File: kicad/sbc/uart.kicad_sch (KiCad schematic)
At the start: 11 parts, among them J2 DB9, U5 74LS06, U6 16550, U8 MAX232, X2 OSC

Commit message: complete schematics
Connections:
- net ~{JOYPORT_ENABLE}: now reaches U6.38 (~{OUT1})
- no-connect marks 11 -> 10
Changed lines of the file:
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@@
   )
   (no_connect (at 157.48 63.5))
-  (no_connect (at 157.48 60.96))
   (no_connect (at 52.07 92.71))
   (no_connect (at 240.03 137.16))
@@
     (stroke (width 0) (type default))
   )
+  (wire (pts (xy 157.48 60.96) (xy 160.02 60.96))
+    (stroke (width 0) (type default))
+  )
   (wire (pts (xy 245.11 54.61) (xy 250.19 54.61))
     (stroke (width 0) (type default))
@@
     (effects (font (size 1.27 1.27)) (justify left))
   )
+  (hierarchical_label "~{JOYPORT_ENABLE}" (shape output) (at 160.02 60.96 0) (fields_autoplaced)
+    (effects (font (size 1.27 1.27)) (justify left))
+  )

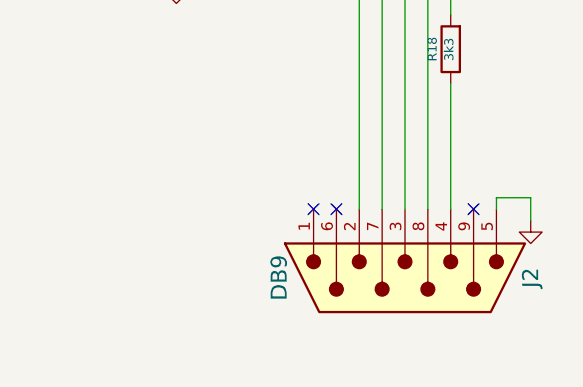
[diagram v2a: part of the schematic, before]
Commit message: fix ERC messages
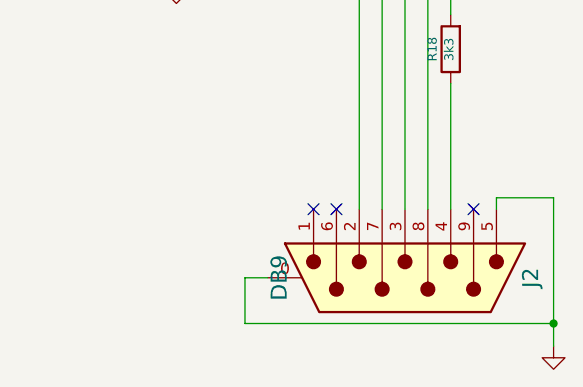
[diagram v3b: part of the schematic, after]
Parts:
- J2: symbol Connector:DB9_Male -> Connector:DE9_Plug_MountingHoles
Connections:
- net GND: now also J2.0 (PAD)
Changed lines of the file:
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@@
   (junction (at 224.79 46.99) (diameter 0) (color 0 0 0 0)
+  )
+  (junction (at 266.7 149.86) (diameter 0) (color 0 0 0 0)
   )
   (junction (at 255.27 67.31) (diameter 0) (color 0 0 0 0)
@@
     (stroke (width 0) (type default))
   )
+  (wire (pts (xy 232.41 149.86) (xy 266.7 149.86))
+    (stroke (width 0) (type default))
+  )
   (wire (pts (xy 224.79 44.45) (xy 224.79 46.99))
     (stroke (width 0) (type default))
@@
     (stroke (width 0) (type default))
   )
+  (wire (pts (xy 266.7 149.86) (xy 266.7 152.4))
+    (stroke (width 0) (type default))
+  )
   (wire (pts (xy 245.11 54.61) (xy 250.19 54.61))
     (stroke (width 0) (type default))
@@
     (stroke (width 0) (type default))
   )
-  (wire (pts (xy 260.35 135.89) (xy 264.16 135.89))
+  (wire (pts (xy 260.35 135.89) (xy 266.7 135.89))
     (stroke (width 0) (type default))
   )
@@
     (stroke (width 0) (type default))
   )
+  (wire (pts (xy 234.95 144.78) (xy 232.41 144.78))
+    (stroke (width 0) (type default))
+  )
   (wire (pts (xy 63.5 130.81) (xy 73.66 130.81))
     (stroke (width 0) (type default))
@@
     (stroke (width 0) (type default))
   )
+  (wire (pts (xy 232.41 144.78) (xy 232.41 149.86))
+    (stroke (width 0) (type default))
+  )
   (wire (pts (xy 106.68 76.2) (xy 95.25 76.2))
     (stroke (width 0) (type default))
@@
     (stroke (width 0) (type default))
   )
-  (wire (pts (xy 264.16 135.89) (xy 264.16 138.43))
+  (wire (pts (xy 266.7 135.89) (xy 266.7 149.86))
     (stroke (width 0) (type default))
   )
@@
     (effects (font (size 1.27 1.27)) (justify left))
   )
-  (symbol (lib_name "VCC_4") (lib_id "power:VCC") (at 73.66 115.57 0) (unit 1)
+  (symbol (lib_id "power:VCC") (at 73.66 115.57 0) (unit 1)
     (in_bom yes) (on_board yes) (dnp no)
     (property "Reference" "#PWR0144" (at 73.66 113.03 0)
@@
     )
   )
-  (symbol (lib_name "GND_2") (lib_id "power:GND") (at 259.08 76.2 0) (unit 1)
+  (symbol (lib_id "power:GND") (at 259.08 76.2 0) (unit 1)
     (in_bom yes) (on_board yes) (dnp no)
     (property "Reference" "#PWR0148" (at 259.08 76.2 0)
@@
     )
   )
-  (symbol (lib_name "VCC_2") (lib_id "power:VCC") (at 224.79 44.45 0) (unit 1)
+  (symbol (lib_id "power:VCC") (at 224.79 44.45 0) (unit 1)
     (in_bom yes) (on_board yes) (dnp no)
     (property "Reference" "#PWR0150" (at 224.79 41.91 0)
@@
     )
   )
-  (symbol (lib_name "GND_3") (lib_id "power:GND") (at 224.79 111.76 0) (unit 1)
+  (symbol (lib_id "power:GND") (at 224.79 111.76 0) (unit 1)
     (in_bom yes) (on_board yes) (dnp no)
     (property "Reference" "#PWR0149" (at 224.79 111.76 0)
@@
     )
   )
-  (symbol (lib_name "GND_1") (lib_id "power:GND") (at 132.08 120.65 0) (unit 1)
+  (symbol (lib_id "power:GND") (at 132.08 120.65 0) (unit 1)
     (in_bom yes) (on_board yes) (dnp no)
     (property "Reference" "#PWR0147" (at 132.08 120.65 0)
@@
     )
   )
-  (symbol (lib_name "VCC_3") (lib_id "power:VCC") (at 95.25 74.93 0) (unit 1)
+  (symbol (lib_id "power:VCC") (at 95.25 74.93 0) (unit 1)
     (in_bom yes) (on_board yes) (dnp no)
     (property "Reference" "#PWR0145" (at 95.25 72.39 0)
@@
     )
   )
-  (symbol (lib_name "GND_4") (lib_id "power:GND") (at 264.16 138.43 0) (unit 1)
-    (in_bom yes) (on_board yes) (dnp no)
-    (property "Reference" "#PWR0139" (at 264.16 138.43 0)
-      (effects (font (size 0.762 0.762)) hide)
-    )
-    (property "Value" "GND" (at 264.16 140.208 0)
-      (effects (font (size 0.762 0.762)) hide)
-    )
-    (property "Footprint" "" (at 264.16 138.43 0)
-      (effects (font (size 1.27 1.27)) hide)
-    )
-    (property "Datasheet" "" (at 264.16 138.43 0)
+  (symbol (lib_id "power:GND") (at 266.7 152.4 0) (unit 1)
+    (in_bom yes) (on_board yes) (dnp no)
+    (property "Reference" "#PWR0139" (at 266.7 152.4 0)
+      (effects (font (size 0.762 0.762)) hide)
+    )
+    (property "Value" "GND" (at 266.7 154.178 0)
+      (effects (font (size 0.762 0.762)) hide)
+    )
+    (property "Footprint" "" (at 266.7 152.4 0)
+      (effects (font (size 1.27 1.27)) hide)
+    )
+    (property "Datasheet" "" (at 266.7 152.4 0)
       (effects (font (size 1.27 1.27)) hide)
     )
@@
     )
   )
-  (symbol (lib_name "VCC_1") (lib_id "power:VCC") (at 132.08 29.21 0) (unit 1)
+  (symbol (lib_id "power:VCC") (at 132.08 29.21 0) (unit 1)
     (in_bom yes) (on_board yes) (dnp no)
     (property "Reference" "#PWR0146" (at 132.08 26.67 0)
@@
     )
   )
-  (symbol (lib_id "Connector:DB9_Male") (at 250.19 144.78 270) (unit 1)
+  (symbol (lib_id "Connector:DE9_Plug_MountingHoles") (at 250.19 144.78 270) (unit 1)
     (in_bom yes) (on_board yes) (dnp no)
     (property "Reference" "J2" (at 264.16 144.78 0)
@@
       (effects (font (size 1.27 1.27)) hide)
     )
+    (pin "0")
     (pin "1")
     (pin "2")

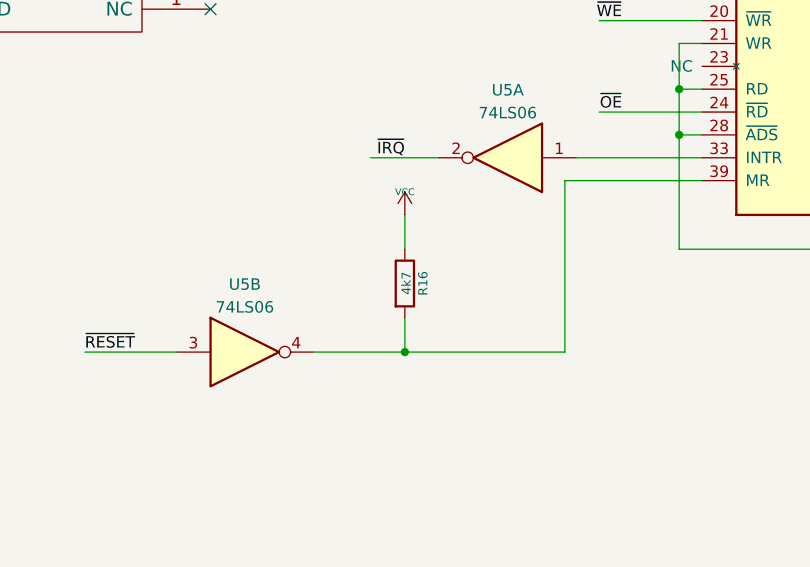
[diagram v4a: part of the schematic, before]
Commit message: fix some ugly routin
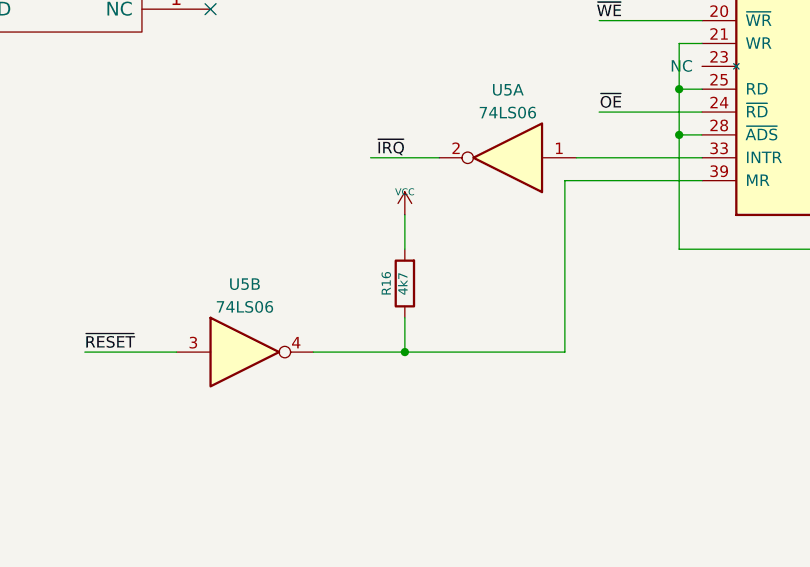
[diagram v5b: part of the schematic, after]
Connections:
- net VCC: now also R16.2; no longer R16.1
- net at U5.4, U6.39 (MR): now also R16.1; no longer R16.2
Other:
- moved on the sheet: R16
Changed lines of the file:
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@@
     )
   )
-  (symbol (lib_id "Device:R") (at 73.66 123.19 0) (unit 1)
+  (symbol (lib_id "Device:R") (at 73.66 123.19 180) (unit 1)
     (in_bom yes) (on_board yes) (dnp no)
-    (property "Reference" "R16" (at 75.692 123.19 90)
+    (property "Reference" "R16" (at 71.628 123.19 90)
       (effects (font (size 1.016 1.016)))
     )
-    (property "Value" "4k7" (at 73.8378 123.1646 90)
+    (property "Value" "4k7" (at 73.4822 123.2154 90)
       (effects (font (size 1.016 1.016)))
     )
-    (property "Footprint" "Resistor_THT:R_Axial_DIN0204_L3.6mm_D1.6mm_P5.08mm_Horizontal" (at 71.882 123.19 90)
+    (property "Footprint" "Resistor_THT:R_Axial_DIN0204_L3.6mm_D1.6mm_P5.08mm_Horizontal" (at 75.438 123.19 90)
       (effects (font (size 1.27 1.27)) hide)
     )

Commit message: moved all symbols into custom library
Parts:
- C19, C21, C22, C25: footprint Capacitor_THT:CP_Radial_D4.0mm_P2.00mm -> Capacitor_THT:CP_Radial_D10.0mm_P5.00mm; symbol Device:C_Polarized -> steckschwein:C_Polarized
- J2: symbol Connector:DE9_Plug_MountingHoles -> steckschwein:DE9_Plug_MountingHoles
- R16, R18: symbol Device:R -> steckschwein:R
- U5: symbol 74xx:74LS06 -> steckschwein:74LS06
- U6: symbol UART:16550 -> steckschwein:16550
- U8: symbol Interface_UART:MAX232 -> steckschwein:MAX232
- X2: symbol osc:OSC -> steckschwein:OSC
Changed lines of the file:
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@@
     )
   )
-  (symbol (lib_id "UART:16550") (at 132.08 76.2 0) (unit 1)
+  (symbol (lib_id "steckschwein:16550") (at 132.08 76.2 0) (unit 1)
     (in_bom yes) (on_board yes) (dnp no) (fields_autoplaced)
     (property "Reference" "U6" (at 134.0994 33.1302 0)
@@
     )
   )
-  (symbol (lib_id "74xx:74LS06") (at 85.09 109.22 180) (unit 1)
+  (symbol (lib_id "steckschwein:74LS06") (at 85.09 109.22 180) (unit 1)
     (in_bom yes) (on_board yes) (dnp no) (fields_autoplaced)
     (property "Reference" "U5" (at 85.09 101.7102 0)
@@
     )
   )
-  (symbol (lib_id "74xx:74LS06") (at 55.88 130.81 0) (unit 2)
+  (symbol (lib_id "steckschwein:74LS06") (at 55.88 130.81 0) (unit 2)
     (in_bom yes) (on_board yes) (dnp no) (fields_autoplaced)
     (property "Reference" "U5" (at 55.88 123.3002 0)
@@
     )
   )
-  (symbol (lib_id "Device:C_Polarized") (at 260.35 67.31 270) (unit 1)
+  (symbol (lib_id "steckschwein:C_Polarized") (at 260.35 67.31 270) (unit 1)
     (in_bom yes) (on_board yes) (dnp no)
     (property "Reference" "C25" (at 262.89 67.31 0)
@@
       (effects (font (size 1.016 1.016)) (justify left))
     )
-    (property "Footprint" "Capacitor_THT:CP_Radial_D4.0mm_P2.00mm" (at 256.54 68.2752 0)
+    (property "Footprint" "Capacitor_THT:CP_Radial_D10.0mm_P5.00mm" (at 256.54 68.2752 0)
       (effects (font (size 1.27 1.27)) hide)
     )
@@
     )
   )
-  (symbol (lib_id "Device:C_Polarized") (at 189.23 58.42 0) (unit 1)
+  (symbol (lib_id "steckschwein:C_Polarized") (at 189.23 58.42 0) (unit 1)
     (in_bom yes) (on_board yes) (dnp no)
     (property "Reference" "C19" (at 189.23 55.88 0)
@@
       (effects (font (size 1.016 1.016)) (justify left))
     )
-    (property "Footprint" "Capacitor_THT:CP_Radial_D4.0mm_P2.00mm" (at 190.1952 62.23 0)
+    (property "Footprint" "Capacitor_THT:CP_Radial_D10.0mm_P5.00mm" (at 190.1952 62.23 0)
       (effects (font (size 1.27 1.27)) hide)
     )
@@
     )
   )
-  (symbol (lib_id "osc:OSC") (at 34.29 88.9 0) (unit 1)
+  (symbol (lib_id "steckschwein:OSC") (at 34.29 88.9 0) (unit 1)
     (in_bom yes) (on_board yes) (dnp no)
     (property "Reference" "X2" (at 34.29 81.28 0)
@@
     )
   )
-  (symbol (lib_id "Device:R") (at 255.27 119.38 180) (unit 1)
+  (symbol (lib_id "steckschwein:R") (at 255.27 119.38 180) (unit 1)
     (in_bom yes) (on_board yes) (dnp no)
     (property "Reference" "R18" (at 253.238 119.38 90)
@@
     )
     (property "Footprint" "Resistor_THT:R_Axial_DIN0204_L3.6mm_D1.6mm_P5.08mm_Horizontal" (at 257.048 119.38 90)
-      (effects (font (size 1.27 1.27)) hide)
+      (effects (font (size 0.762 0.762)) hide)
     )
     (property "Datasheet" "~" (at 255.27 119.38 0)
-      (effects (font (size 1.27 1.27)) hide)
+      (effects (font (size 0.762 0.762)))
     )
     (pin "1")
@@
     )
   )
-  (symbol (lib_id "Device:C_Polarized") (at 250.19 74.93 270) (unit 1)
+  (symbol (lib_id "steckschwein:C_Polarized") (at 250.19 74.93 270) (unit 1)
     (in_bom yes) (on_board yes) (dnp no)
     (property "Reference" "C22" (at 252.73 74.93 0)
@@
       (effects (font (size 1.016 1.016)) (justify left))
     )
-    (property "Footprint" "Capacitor_THT:CP_Radial_D4.0mm_P2.00mm" (at 246.38 75.8952 0)
+    (property "Footprint" "Capacitor_THT:CP_Radial_D10.0mm_P5.00mm" (at 246.38 75.8952 0)
       (effects (font (size 1.27 1.27)) hide)
     )
@@
     )
   )
-  (symbol (lib_id "Device:R") (at 73.66 123.19 180) (unit 1)
+  (symbol (lib_id "steckschwein:R") (at 73.66 123.19 180) (unit 1)
     (in_bom yes) (on_board yes) (dnp no)
     (property "Reference" "R16" (at 71.628 123.19 90)
@@
     )
     (property "Footprint" "Resistor_THT:R_Axial_DIN0204_L3.6mm_D1.6mm_P5.08mm_Horizontal" (at 75.438 123.19 90)
-      (effects (font (size 1.27 1.27)) hide)
+      (effects (font (size 0.762 0.762)) hide)
     )
     (property "Datasheet" "~" (at 73.66 123.19 0)
-      (effects (font (size 1.27 1.27)) hide)
+      (effects (font (size 0.762 0.762)))
     )
     (pin "1")
@@
     )
   )
-  (symbol (lib_id "Connector:DE9_Plug_MountingHoles") (at 250.19 144.78 270) (unit 1)
+  (symbol (lib_id "steckschwein:DE9_Plug_MountingHoles") (at 250.19 144.78 270) (unit 1)
     (in_bom yes) (on_board yes) (dnp no)
     (property "Reference" "J2" (at 264.16 144.78 0)
@@
     )
   )
-  (symbol (lib_id "Interface_UART:MAX232") (at 224.79 77.47 0) (unit 1)
+  (symbol (lib_id "steckschwein:MAX232") (at 224.79 77.47 0) (unit 1)
     (in_bom yes) (on_board yes) (dnp no)
     (property "Reference" "U8" (at 224.79 55.88 0)
@@
     )
   )
-  (symbol (lib_id "Device:C_Polarized") (at 250.19 58.42 0) (unit 1)
+  (symbol (lib_id "steckschwein:C_Polarized") (at 250.19 58.42 0) (unit 1)
     (in_bom yes) (on_board yes) (dnp no)
     (property "Reference" "C21" (at 250.19 55.88 0)
@@
       (effects (font (size 1.016 1.016)) (justify left))
     )
-    (property "Footprint" "Capacitor_THT:CP_Radial_D4.0mm_P2.00mm" (at 251.1552 62.23 0)
-      (effects (font (size 1.27 1.27)) hide)
-    )
+    (property "Footprint" "Capacitor_THT:CP_Radial_D10.0mm_P5.00mm" (at 251.1552 62.23 0)
+      (effects (font (size 1.27 1.27)) hide)
+    )

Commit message: moved all footprints into local library
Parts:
- C19, C21, C22, C25: footprint Capacitor_THT:CP_Radial_D10.0mm_P5.00mm -> steckschwein:CP_Radial_D4.0mm_P2.00mm
- J2: footprint Connector_Dsub:DSUB-9_Male_Horizontal_P2.77x2.84mm_EdgePinOffset4.94mm_Housed_MountingHolesOffset7.48mm -> steckschwein:DSUB-9_Male_Horizontal_P2.77x2.84mm_EdgePinOffset4.94mm_Housed_MountingHolesOffset7.48mm
- R16, R18: footprint Resistor_THT:R_Axial_DIN0204_L3.6mm_D1.6mm_P5.08mm_Horizontal -> steckschwein:R_Axial_DIN0204_L3.6mm_D1.6mm_P7.62mm_Horizontal
- U5: footprint Package_DIP:DIP-14_W7.62mm_LongPads -> steckschwein:DIP-14_W7.62mm_LongPads
- U6: footprint Package_LCC:PLCC-44_THT-Socket -> steckschwein:PLCC-44_THT-Socket
- U8: footprint Package_DIP:DIP-16_W7.62mm_LongPads -> steckschwein:DIP-16_W7.62mm_LongPads
- X2: footprint Oscillator:Oscillator_DIP-14_LargePads -> steckschwein:Oscillator_DIP-14_LargePads
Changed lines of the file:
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@@
       (effects (font (size 1.27 1.27)) (justify left))
     )
-    (property "Footprint" "Package_LCC:PLCC-44_THT-Socket" (at 132.08 76.2 0)
+    (property "Footprint" "steckschwein:PLCC-44_THT-Socket" (at 132.08 76.2 0)
       (effects (font (size 1.27 1.27) italic) hide)
     )
@@
       (effects (font (size 1.27 1.27)))
     )
-    (property "Footprint" "Package_DIP:DIP-14_W7.62mm_LongPads" (at 85.09 109.22 0)
+    (property "Footprint" "steckschwein:DIP-14_W7.62mm_LongPads" (at 85.09 109.22 0)
       (effects (font (size 1.27 1.27)) hide)
     )
@@
       (effects (font (size 1.27 1.27)))
     )
-    (property "Footprint" "Package_DIP:DIP-14_W7.62mm_LongPads" (at 55.88 130.81 0)
+    (property "Footprint" "steckschwein:DIP-14_W7.62mm_LongPads" (at 55.88 130.81 0)
       (effects (font (size 1.27 1.27)) hide)
     )
@@
       (effects (font (size 1.016 1.016)) (justify left))
     )
-    (property "Footprint" "Capacitor_THT:CP_Radial_D10.0mm_P5.00mm" (at 256.54 68.2752 0)
+    (property "Footprint" "steckschwein:CP_Radial_D4.0mm_P2.00mm" (at 256.54 68.2752 0)
       (effects (font (size 1.27 1.27)) hide)
     )
@@
       (effects (font (size 1.016 1.016)) (justify left))
     )
-    (property "Footprint" "Capacitor_THT:CP_Radial_D10.0mm_P5.00mm" (at 190.1952 62.23 0)
+    (property "Footprint" "steckschwein:CP_Radial_D4.0mm_P2.00mm" (at 190.1952 62.23 0)
       (effects (font (size 1.27 1.27)) hide)
     )
@@
       (effects (font (size 1.778 1.778)))
     )
-    (property "Footprint" "Oscillator:Oscillator_DIP-14_LargePads" (at 34.29 88.9 0)
+    (property "Footprint" "steckschwein:Oscillator_DIP-14_LargePads" (at 34.29 88.9 0)
       (effects (font (size 1.524 1.524)) hide)
     )
@@
       (effects (font (size 1.016 1.016)))
     )
-    (property "Footprint" "Resistor_THT:R_Axial_DIN0204_L3.6mm_D1.6mm_P5.08mm_Horizontal" (at 257.048 119.38 90)
+    (property "Footprint" "steckschwein:R_Axial_DIN0204_L3.6mm_D1.6mm_P7.62mm_Horizontal" (at 257.048 119.38 90)
       (effects (font (size 0.762 0.762)) hide)
     )
@@
       (effects (font (size 1.016 1.016)) (justify left))
     )
-    (property "Footprint" "Capacitor_THT:CP_Radial_D10.0mm_P5.00mm" (at 246.38 75.8952 0)
+    (property "Footprint" "steckschwein:CP_Radial_D4.0mm_P2.00mm" (at 246.38 75.8952 0)
       (effects (font (size 1.27 1.27)) hide)
     )
@@
       (effects (font (size 1.016 1.016)))
     )
-    (property "Footprint" "Resistor_THT:R_Axial_DIN0204_L3.6mm_D1.6mm_P5.08mm_Horizontal" (at 75.438 123.19 90)
+    (property "Footprint" "steckschwein:R_Axial_DIN0204_L3.6mm_D1.6mm_P7.62mm_Horizontal" (at 75.438 123.19 90)
       (effects (font (size 0.762 0.762)) hide)
     )
@@
       (effects (font (size 1.778 1.778)))
     )
-    (property "Footprint" "Connector_Dsub:DSUB-9_Male_Horizontal_P2.77x2.84mm_EdgePinOffset4.94mm_Housed_MountingHolesOffset7.48mm" (at 250.19 144.78 0)
+    (property "Footprint" "steckschwein:DSUB-9_Male_Horizontal_P2.77x2.84mm_EdgePinOffset4.94mm_Housed_MountingHolesOffset7.48mm" (at 250.19 144.78 0)
       (effects (font (size 1.27 1.27)) hide)
     )
@@
       (effects (font (size 1.778 1.778)))
     )
-    (property "Footprint" "Package_DIP:DIP-16_W7.62mm_LongPads" (at 226.06 104.14 0)
+    (property "Footprint" "steckschwein:DIP-16_W7.62mm_LongPads" (at 226.06 104.14 0)
       (effects (font (size 1.27 1.27)) (justify left) hide)
     )
@@
       (effects (font (size 1.016 1.016)) (justify left))
     )
-    (property "Footprint" "Capacitor_THT:CP_Radial_D10.0mm_P5.00mm" (at 251.1552 62.23 0)
-      (effects (font (size 1.27 1.27)) hide)
-    )
+    (property "Footprint" "steckschwein:CP_Radial_D4.0mm_P2.00mm" (at 251.1552 62.23 0)
+      (effects (font (size 1.27 1.27)) hide)
+    )

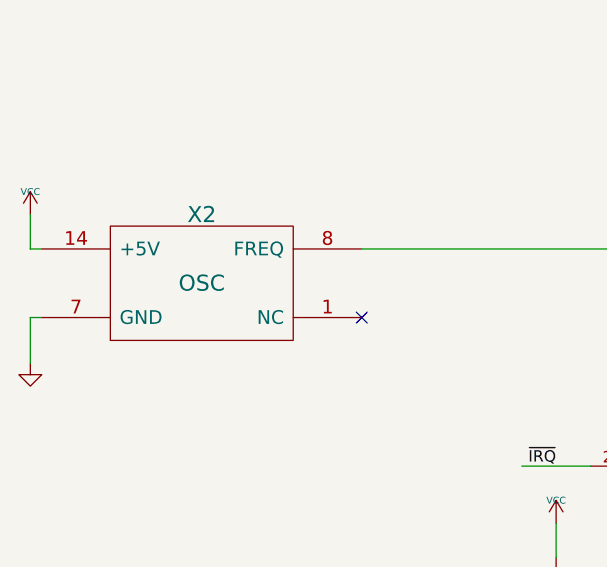
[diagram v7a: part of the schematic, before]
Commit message: component values/units cleanup
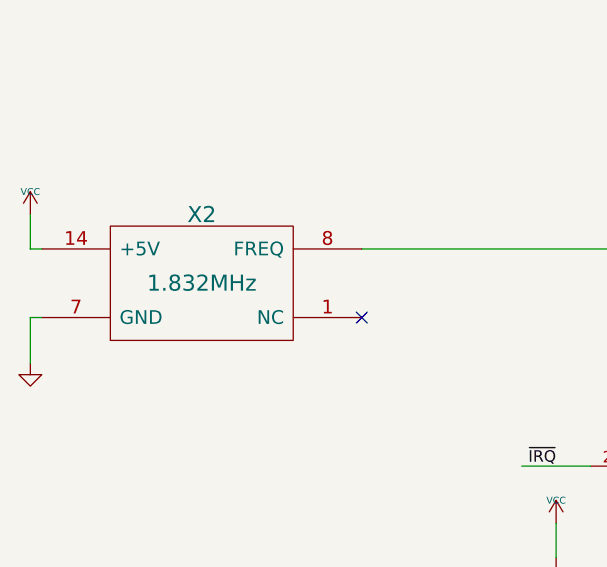
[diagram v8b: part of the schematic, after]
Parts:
- X2: value OSC -> 1.832MHz
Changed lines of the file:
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@@
       (effects (font (size 1.778 1.778)))
     )
-    (property "Value" "OSC" (at 34.29 88.9 0)
+    (property "Value" "1.832MHz" (at 34.29 88.9 0)
       (effects (font (size 1.778 1.778)))
     )
